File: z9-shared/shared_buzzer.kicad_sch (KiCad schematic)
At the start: 6 parts

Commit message: x
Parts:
- gave numbers to parts that had none: 6
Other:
- note added: "700 series"
- note added: "do not annotate - intended to be shared"
- note removed: "do not annotate - intended to nbe shared"
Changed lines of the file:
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@@
 		(title "l8")
 	)
-	(text "do not annotate - intended to nbe shared"
+	(text "700 series "
+		(exclude_from_sim no)
+		(at 125.222 132.334 0)
+		(effects
+			(font
+				(size 1.27 1.27)
+			)
+		)
+	)
+	(text "do not annotate - intended to be shared"
 		(exclude_from_sim no)
 		(at 159.258 131.064 0)
@@
 		(dnp no)
 		(fields_autoplaced yes)
-		(property "Reference" "Q?"
+		(property "Reference" "Q701"
 			(at 153.67 97.7899 0)
 			(effects
@@
 				)
 			)
-			(project "z9-console"
-				(path "/8d063f79-9282-4820-bcf4-1ff3c006cf08/8d0cf1ff-dd45-490a-9f6d-ad4eb4a5c201"
-					(reference "Q?")
+			(project "z9-pdm"
+				(path "/8d063f79-9282-4820-bcf4-1ff3c006cf08/c97401c5-7e03-4d93-a14f-f692468677b5"
+					(reference "Q701")
 					(unit 1)
 				)
@@
 		(dnp no)
 		(fields_autoplaced yes)
-		(property "Reference" "D?"
+		(property "Reference" "D701"
 			(at 139.7 79.6924 0)
 			(effects
@@
 				)
 			)
-			(project "z9-console"
-				(path "/8d063f79-9282-4820-bcf4-1ff3c006cf08/8d0cf1ff-dd45-490a-9f6d-ad4eb4a5c201"
-					(reference "D?")
+			(project "z9-pdm"
+				(path "/8d063f79-9282-4820-bcf4-1ff3c006cf08/c97401c5-7e03-4d93-a14f-f692468677b5"
+					(reference "D701")
 					(unit 1)
 				)
@@
 		(dnp no)
 		(fields_autoplaced yes)
-		(property "Reference" "#PWR0103"
+		(property "Reference" "#PWR0701"
 			(at 127 120.65 0)
 			(effects
@@
 				)
 			)
-			(project "z9-console"
-				(path "/8d063f79-9282-4820-bcf4-1ff3c006cf08/8d0cf1ff-dd45-490a-9f6d-ad4eb4a5c201"
-					(reference "#PWR?")
+			(project "z9-pdm"
+				(path "/8d063f79-9282-4820-bcf4-1ff3c006cf08/c97401c5-7e03-4d93-a14f-f692468677b5"
+					(reference "#PWR0701")
 					(unit 1)
 				)
@@
 		(dnp no)
 		(fields_autoplaced yes)
-		(property "Reference" "#PWR0102"
+		(property "Reference" "#PWR0702"
 			(at 149.86 72.39 0)
 			(effects
@@
 				)
 			)
-			(project "z9-console"
-				(path "/8d063f79-9282-4820-bcf4-1ff3c006cf08/8d0cf1ff-dd45-490a-9f6d-ad4eb4a5c201"
-					(reference "#PWR?")
+			(project "z9-pdm"
+				(path "/8d063f79-9282-4820-bcf4-1ff3c006cf08/c97401c5-7e03-4d93-a14f-f692468677b5"
+					(reference "#PWR0702")
 					(unit 1)
 				)
@@
 		(on_board yes)
 		(dnp no)
-		(property "Reference" "C?"
+		(property "Reference" "C701"
 			(at 129.54 77.47 90)
 			(effects
@@
 				)
 			)
-			(project "z9-console"
-				(path "/8d063f79-9282-4820-bcf4-1ff3c006cf08/8d0cf1ff-dd45-490a-9f6d-ad4eb4a5c201"
-					(reference "C?")
+			(project "z9-pdm"
+				(path "/8d063f79-9282-4820-bcf4-1ff3c006cf08/c97401c5-7e03-4d93-a14f-f692468677b5"
+					(reference "C701")
 					(unit 1)
 				)
@@
 		(dnp no)
 		(fields_autoplaced yes)
-		(property "Reference" "BZ?"
+		(property "Reference" "BZ701"
 			(at 156.21 78.7399 0)
 			(effects
@@
 				)
 			)
-			(project "z9-console"
-				(path "/8d063f79-9282-4820-bcf4-1ff3c006cf08/8d0cf1ff-dd45-490a-9f6d-ad4eb4a5c201"
-					(reference "BZ?")
+			(project "z9-pdm"
+				(path "/8d063f79-9282-4820-bcf4-1ff3c006cf08/c97401c5-7e03-4d93-a14f-f692468677b5"
+					(reference "BZ701")
 					(unit 1)
 				)
@@
 		(on_board yes)
 		(dnp no)
-		(property "Reference" "R?"
+		(property "Reference" "R704"
 			(at 129.032 110.49 90)
 			(effects
@@
 				)
 			)
-			(project "z9-console"
-				(path "/8d063f79-9282-4820-bcf4-1ff3c006cf08/8d0cf1ff-dd45-490a-9f6d-ad4eb4a5c201"
-					(reference "R?")
+			(project "z9-pdm"
+				(path "/8d063f79-9282-4820-bcf4-1ff3c006cf08/c97401c5-7e03-4d93-a14f-f692468677b5"
+					(reference "R704")
 					(unit 1)
 				)
@@
 		(on_board yes)
 		(dnp no)
-		(property "Reference" "R?"
+		(property "Reference" "R703"
 			(at 121.92 101.6 90)
 			(effects
@@
 				)
 			)
-			(project "z9-console"
-				(path "/8d063f79-9282-4820-bcf4-1ff3c006cf08/8d0cf1ff-dd45-490a-9f6d-ad4eb4a5c201"
-					(reference "R?")
+			(project "z9-pdm"
+				(path "/8d063f79-9282-4820-bcf4-1ff3c006cf08/c97401c5-7e03-4d93-a14f-f692468677b5"
+					(reference "R703")
 					(unit 1)
 				)
@@
 		(dnp no)
 		(fields_autoplaced yes)
-		(property "Reference" "#PWR0101"
+		(property "Reference" "#PWR0703"
 			(at 149.86 119.38 0)
 			(effects
@@
 				)
 			)
-			(project "z9-console"
-				(path "/8d063f79-9282-4820-bcf4-1ff3c006cf08/8d0cf1ff-dd45-490a-9f6d-ad4eb4a5c201"
-					(reference "#PWR?")
-					(unit 1)
-				)
+			(project "z9-pdm"
+				(path "/8d063f79-9282-4820-bcf4-1ff3c006cf08/c97401c5-7e03-4d93-a14f-f692468677b5"
+					(reference "#PWR0703")
+					(unit 1)
+				)

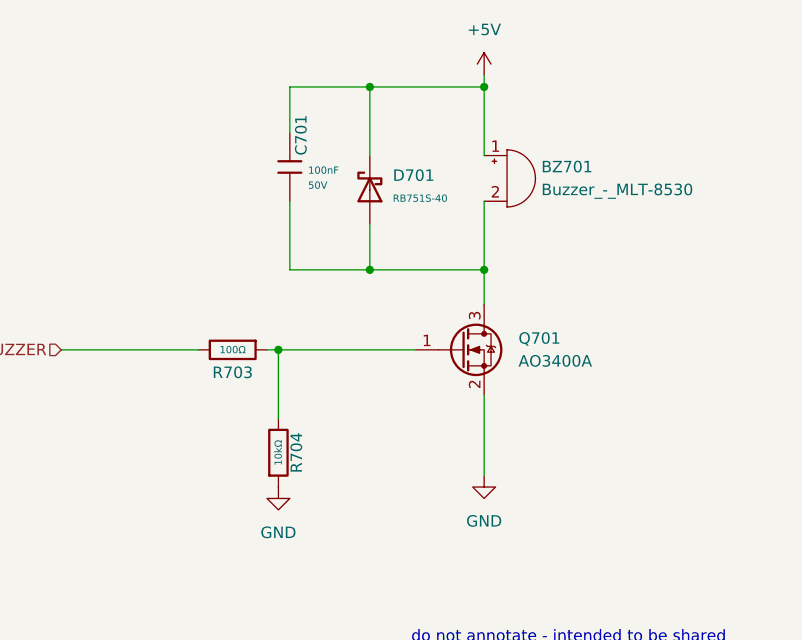
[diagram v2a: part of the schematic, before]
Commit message: lcd power switch-- add new accelerometer
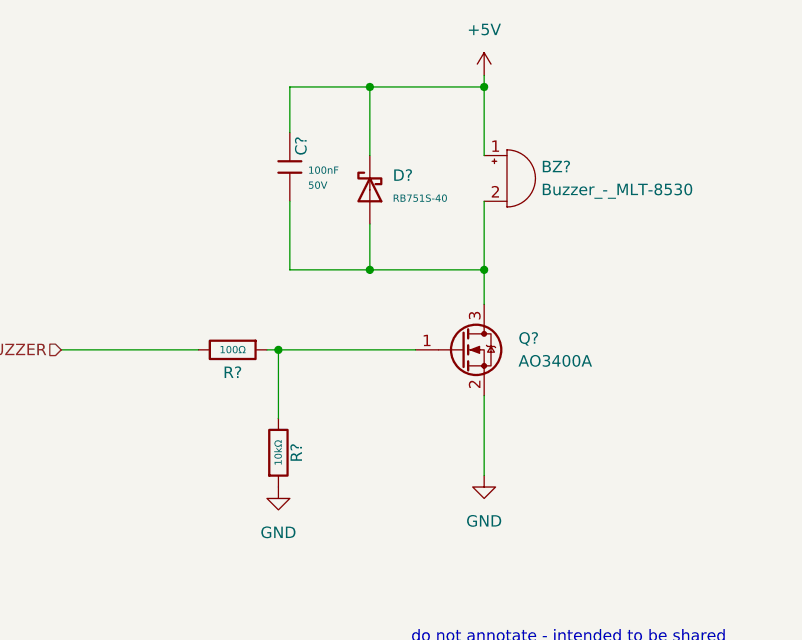
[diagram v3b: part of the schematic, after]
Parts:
- renumbered BZ701 to BZ?, C701 to C?, D701 to D?, Q701 to Q?, R704 to R?, R703 to R?
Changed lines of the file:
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@@
 		(dnp no)
 		(fields_autoplaced yes)
-		(property "Reference" "Q701"
+		(property "Reference" "Q?"
 			(at 153.67 97.7899 0)
 			(effects
@@
 				)
 			)
-			(project "z9-pdm"
-				(path "/8d063f79-9282-4820-bcf4-1ff3c006cf08/c97401c5-7e03-4d93-a14f-f692468677b5"
-					(reference "Q701")
+			(project "z9-console"
+				(path "/8d063f79-9282-4820-bcf4-1ff3c006cf08/8d0cf1ff-dd45-490a-9f6d-ad4eb4a5c201"
+					(reference "Q?")
 					(unit 1)
 				)
@@
 		(dnp no)
 		(fields_autoplaced yes)
-		(property "Reference" "D701"
+		(property "Reference" "D?"
 			(at 139.7 79.6924 0)
 			(effects
@@
 				)
 			)
-			(project "z9-pdm"
-				(path "/8d063f79-9282-4820-bcf4-1ff3c006cf08/c97401c5-7e03-4d93-a14f-f692468677b5"
-					(reference "D701")
+			(project "z9-console"
+				(path "/8d063f79-9282-4820-bcf4-1ff3c006cf08/8d0cf1ff-dd45-490a-9f6d-ad4eb4a5c201"
+					(reference "D?")
 					(unit 1)
 				)
@@
 		(dnp no)
 		(fields_autoplaced yes)
-		(property "Reference" "#PWR0701"
+		(property "Reference" "#PWR?"
 			(at 127 120.65 0)
 			(effects
@@
 				)
 			)
-			(project "z9-pdm"
-				(path "/8d063f79-9282-4820-bcf4-1ff3c006cf08/c97401c5-7e03-4d93-a14f-f692468677b5"
-					(reference "#PWR0701")
+			(project "z9-console"
+				(path "/8d063f79-9282-4820-bcf4-1ff3c006cf08/8d0cf1ff-dd45-490a-9f6d-ad4eb4a5c201"
+					(reference "#PWR?")
 					(unit 1)
 				)
@@
 		(dnp no)
 		(fields_autoplaced yes)
-		(property "Reference" "#PWR0702"
+		(property "Reference" "#PWR?"
 			(at 149.86 72.39 0)
 			(effects
@@
 				)
 			)
-			(project "z9-pdm"
-				(path "/8d063f79-9282-4820-bcf4-1ff3c006cf08/c97401c5-7e03-4d93-a14f-f692468677b5"
-					(reference "#PWR0702")
+			(project "z9-console"
+				(path "/8d063f79-9282-4820-bcf4-1ff3c006cf08/8d0cf1ff-dd45-490a-9f6d-ad4eb4a5c201"
+					(reference "#PWR?")
 					(unit 1)
 				)
@@
 		(on_board yes)
 		(dnp no)
-		(property "Reference" "C701"
+		(property "Reference" "C?"
 			(at 129.54 77.47 90)
 			(effects
@@
 				)
 			)
-			(project "z9-pdm"
-				(path "/8d063f79-9282-4820-bcf4-1ff3c006cf08/c97401c5-7e03-4d93-a14f-f692468677b5"
-					(reference "C701")
+			(project "z9-console"
+				(path "/8d063f79-9282-4820-bcf4-1ff3c006cf08/8d0cf1ff-dd45-490a-9f6d-ad4eb4a5c201"
+					(reference "C?")
 					(unit 1)
 				)
@@
 		(dnp no)
 		(fields_autoplaced yes)
-		(property "Reference" "BZ701"
+		(property "Reference" "BZ?"
 			(at 156.21 78.7399 0)
 			(effects
@@
 				)
 			)
-			(project "z9-pdm"
-				(path "/8d063f79-9282-4820-bcf4-1ff3c006cf08/c97401c5-7e03-4d93-a14f-f692468677b5"
-					(reference "BZ701")
+			(project "z9-console"
+				(path "/8d063f79-9282-4820-bcf4-1ff3c006cf08/8d0cf1ff-dd45-490a-9f6d-ad4eb4a5c201"
+					(reference "BZ?")
 					(unit 1)
 				)
@@
 		(on_board yes)
 		(dnp no)
-		(property "Reference" "R704"
+		(property "Reference" "R?"
 			(at 129.032 110.49 90)
 			(effects
@@
 				)
 			)
-			(project "z9-pdm"
-				(path "/8d063f79-9282-4820-bcf4-1ff3c006cf08/c97401c5-7e03-4d93-a14f-f692468677b5"
-					(reference "R704")
+			(project "z9-console"
+				(path "/8d063f79-9282-4820-bcf4-1ff3c006cf08/8d0cf1ff-dd45-490a-9f6d-ad4eb4a5c201"
+					(reference "R?")
 					(unit 1)
 				)
@@
 		(on_board yes)
 		(dnp no)
-		(property "Reference" "R703"
+		(property "Reference" "R?"
 			(at 121.92 101.6 90)
 			(effects
@@
 				)
 			)
-			(project "z9-pdm"
-				(path "/8d063f79-9282-4820-bcf4-1ff3c006cf08/c97401c5-7e03-4d93-a14f-f692468677b5"
-					(reference "R703")
+			(project "z9-console"
+				(path "/8d063f79-9282-4820-bcf4-1ff3c006cf08/8d0cf1ff-dd45-490a-9f6d-ad4eb4a5c201"
+					(reference "R?")
 					(unit 1)
 				)
@@
 		(dnp no)
 		(fields_autoplaced yes)
-		(property "Reference" "#PWR0703"
+		(property "Reference" "#PWR?"
 			(at 149.86 119.38 0)
 			(effects
@@
 				)
 			)
-			(project "z9-pdm"
-				(path "/8d063f79-9282-4820-bcf4-1ff3c006cf08/c97401c5-7e03-4d93-a14f-f692468677b5"
-					(reference "#PWR0703")
-					(unit 1)
-				)
+			(project "z9-console"
+				(path "/8d063f79-9282-4820-bcf4-1ff3c006cf08/8d0cf1ff-dd45-490a-9f6d-ad4eb4a5c201"
+					(reference "#PWR?")
+					(unit 1)
+				)

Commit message: change MEMS device
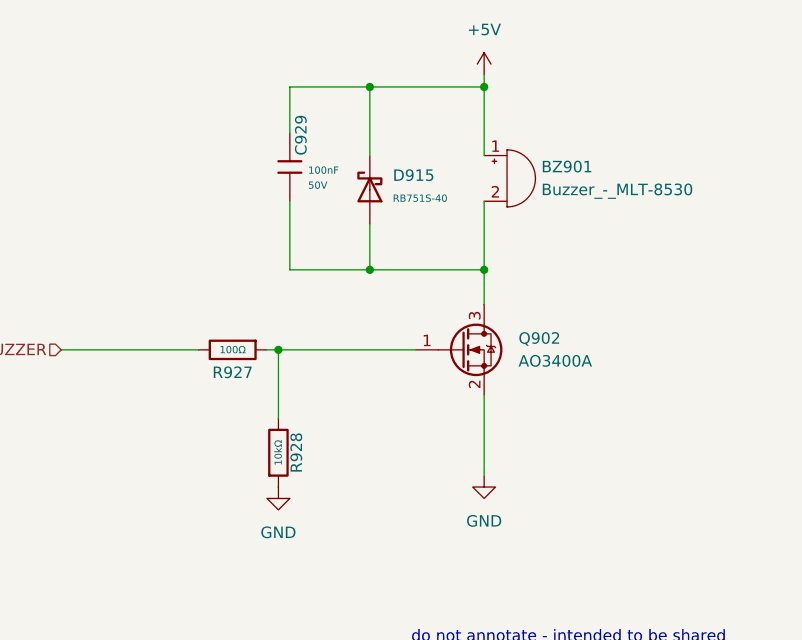
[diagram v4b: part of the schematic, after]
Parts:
- gave numbers to parts that had none: 6
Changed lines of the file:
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@@
 		(dnp no)
 		(fields_autoplaced yes)
-		(property "Reference" "Q?"
+		(property "Reference" "Q902"
 			(at 153.67 97.7899 0)
 			(effects
@@
 			(project "z9-console"
 				(path "/8d063f79-9282-4820-bcf4-1ff3c006cf08/8d0cf1ff-dd45-490a-9f6d-ad4eb4a5c201"
-					(reference "Q?")
+					(reference "Q902")
 					(unit 1)
 				)
@@
 		(dnp no)
 		(fields_autoplaced yes)
-		(property "Reference" "D?"
+		(property "Reference" "D915"
 			(at 139.7 79.6924 0)
 			(effects
@@
 			(project "z9-console"
 				(path "/8d063f79-9282-4820-bcf4-1ff3c006cf08/8d0cf1ff-dd45-490a-9f6d-ad4eb4a5c201"
-					(reference "D?")
+					(reference "D915")
 					(unit 1)
 				)
@@
 		(dnp no)
 		(fields_autoplaced yes)
-		(property "Reference" "#PWR?"
+		(property "Reference" "#PWR0946"
 			(at 127 120.65 0)
 			(effects
@@
 			(project "z9-console"
 				(path "/8d063f79-9282-4820-bcf4-1ff3c006cf08/8d0cf1ff-dd45-490a-9f6d-ad4eb4a5c201"
-					(reference "#PWR?")
+					(reference "#PWR0946")
 					(unit 1)
 				)
@@
 		(dnp no)
 		(fields_autoplaced yes)
-		(property "Reference" "#PWR?"
+		(property "Reference" "#PWR0947"
 			(at 149.86 72.39 0)
 			(effects
@@
 			(project "z9-console"
 				(path "/8d063f79-9282-4820-bcf4-1ff3c006cf08/8d0cf1ff-dd45-490a-9f6d-ad4eb4a5c201"
-					(reference "#PWR?")
+					(reference "#PWR0947")
 					(unit 1)
 				)
@@
 		(on_board yes)
 		(dnp no)
-		(property "Reference" "C?"
+		(property "Reference" "C929"
 			(at 129.54 77.47 90)
 			(effects
@@
 			(project "z9-console"
 				(path "/8d063f79-9282-4820-bcf4-1ff3c006cf08/8d0cf1ff-dd45-490a-9f6d-ad4eb4a5c201"
-					(reference "C?")
+					(reference "C929")
 					(unit 1)
 				)
@@
 		(dnp no)
 		(fields_autoplaced yes)
-		(property "Reference" "BZ?"
+		(property "Reference" "BZ901"
 			(at 156.21 78.7399 0)
 			(effects
@@
 			(project "z9-console"
 				(path "/8d063f79-9282-4820-bcf4-1ff3c006cf08/8d0cf1ff-dd45-490a-9f6d-ad4eb4a5c201"
-					(reference "BZ?")
+					(reference "BZ901")
 					(unit 1)
 				)
@@
 		(on_board yes)
 		(dnp no)
-		(property "Reference" "R?"
+		(property "Reference" "R928"
 			(at 129.032 110.49 90)
 			(effects
@@
 			(project "z9-console"
 				(path "/8d063f79-9282-4820-bcf4-1ff3c006cf08/8d0cf1ff-dd45-490a-9f6d-ad4eb4a5c201"
-					(reference "R?")
+					(reference "R928")
 					(unit 1)
 				)
@@
 		(on_board yes)
 		(dnp no)
-		(property "Reference" "R?"
+		(property "Reference" "R927"
 			(at 121.92 101.6 90)
 			(effects
@@
 			(project "z9-console"
 				(path "/8d063f79-9282-4820-bcf4-1ff3c006cf08/8d0cf1ff-dd45-490a-9f6d-ad4eb4a5c201"
-					(reference "R?")
+					(reference "R927")
 					(unit 1)
 				)
@@
 		(dnp no)
 		(fields_autoplaced yes)
-		(property "Reference" "#PWR?"
+		(property "Reference" "#PWR0948"
 			(at 149.86 119.38 0)
 			(effects
@@
 			(project "z9-console"
 				(path "/8d063f79-9282-4820-bcf4-1ff3c006cf08/8d0cf1ff-dd45-490a-9f6d-ad4eb4a5c201"
-					(reference "#PWR?")
-					(unit 1)
-				)
+					(reference "#PWR0948")
+					(unit 1)
+				)

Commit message: cleanup - change fus as test to shorten vale
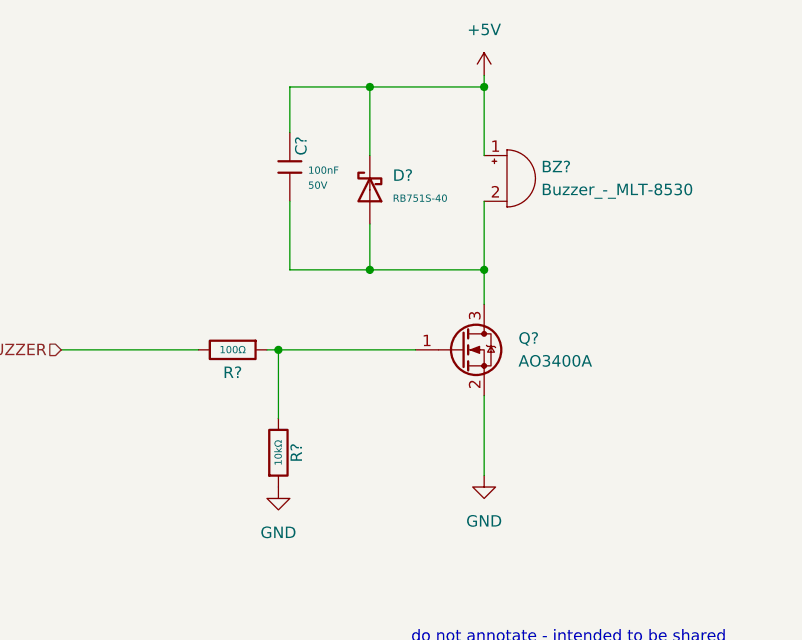
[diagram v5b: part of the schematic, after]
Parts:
- renumbered BZ901 to BZ?, C929 to C?, D915 to D?, Q902 to Q?, R928 to R?, R927 to R?
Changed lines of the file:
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@@
 		(dnp no)
 		(fields_autoplaced yes)
-		(property "Reference" "Q902"
+		(property "Reference" "Q?"
 			(at 153.67 97.7899 0)
 			(effects
@@
 				)
 			)
-			(project "z9-console"
-				(path "/8d063f79-9282-4820-bcf4-1ff3c006cf08/8d0cf1ff-dd45-490a-9f6d-ad4eb4a5c201"
-					(reference "Q902")
+			(project "z9-pdm"
+				(path "/8d063f79-9282-4820-bcf4-1ff3c006cf08/c97401c5-7e03-4d93-a14f-f692468677b5"
+					(reference "Q?")
 					(unit 1)
 				)
@@
 		(dnp no)
 		(fields_autoplaced yes)
-		(property "Reference" "D915"
+		(property "Reference" "D?"
 			(at 139.7 79.6924 0)
 			(effects
@@
 				)
 			)
-			(project "z9-console"
-				(path "/8d063f79-9282-4820-bcf4-1ff3c006cf08/8d0cf1ff-dd45-490a-9f6d-ad4eb4a5c201"
-					(reference "D915")
+			(project "z9-pdm"
+				(path "/8d063f79-9282-4820-bcf4-1ff3c006cf08/c97401c5-7e03-4d93-a14f-f692468677b5"
+					(reference "D?")
 					(unit 1)
 				)
@@
 		(dnp no)
 		(fields_autoplaced yes)
-		(property "Reference" "#PWR0946"
+		(property "Reference" "#PWR?"
 			(at 127 120.65 0)
 			(effects
@@
 				)
 			)
-			(project "z9-console"
-				(path "/8d063f79-9282-4820-bcf4-1ff3c006cf08/8d0cf1ff-dd45-490a-9f6d-ad4eb4a5c201"
-					(reference "#PWR0946")
+			(project "z9-pdm"
+				(path "/8d063f79-9282-4820-bcf4-1ff3c006cf08/c97401c5-7e03-4d93-a14f-f692468677b5"
+					(reference "#PWR?")
 					(unit 1)
 				)
@@
 		(dnp no)
 		(fields_autoplaced yes)
-		(property "Reference" "#PWR0947"
+		(property "Reference" "#PWR?"
 			(at 149.86 72.39 0)
 			(effects
@@
 				)
 			)
-			(project "z9-console"
-				(path "/8d063f79-9282-4820-bcf4-1ff3c006cf08/8d0cf1ff-dd45-490a-9f6d-ad4eb4a5c201"
-					(reference "#PWR0947")
+			(project "z9-pdm"
+				(path "/8d063f79-9282-4820-bcf4-1ff3c006cf08/c97401c5-7e03-4d93-a14f-f692468677b5"
+					(reference "#PWR?")
 					(unit 1)
 				)
@@
 		(on_board yes)
 		(dnp no)
-		(property "Reference" "C929"
+		(property "Reference" "C?"
 			(at 129.54 77.47 90)
 			(effects
@@
 				)
 			)
-			(project "z9-console"
-				(path "/8d063f79-9282-4820-bcf4-1ff3c006cf08/8d0cf1ff-dd45-490a-9f6d-ad4eb4a5c201"
-					(reference "C929")
+			(project "z9-pdm"
+				(path "/8d063f79-9282-4820-bcf4-1ff3c006cf08/c97401c5-7e03-4d93-a14f-f692468677b5"
+					(reference "C?")
 					(unit 1)
 				)
@@
 		(dnp no)
 		(fields_autoplaced yes)
-		(property "Reference" "BZ901"
+		(property "Reference" "BZ?"
 			(at 156.21 78.7399 0)
 			(effects
@@
 				)
 			)
-			(project "z9-console"
-				(path "/8d063f79-9282-4820-bcf4-1ff3c006cf08/8d0cf1ff-dd45-490a-9f6d-ad4eb4a5c201"
-					(reference "BZ901")
+			(project "z9-pdm"
+				(path "/8d063f79-9282-4820-bcf4-1ff3c006cf08/c97401c5-7e03-4d93-a14f-f692468677b5"
+					(reference "BZ?")
 					(unit 1)
 				)
@@
 		(on_board yes)
 		(dnp no)
-		(property "Reference" "R928"
+		(property "Reference" "R?"
 			(at 129.032 110.49 90)
 			(effects
@@
 				)
 			)
-			(project "z9-console"
-				(path "/8d063f79-9282-4820-bcf4-1ff3c006cf08/8d0cf1ff-dd45-490a-9f6d-ad4eb4a5c201"
-					(reference "R928")
+			(project "z9-pdm"
+				(path "/8d063f79-9282-4820-bcf4-1ff3c006cf08/c97401c5-7e03-4d93-a14f-f692468677b5"
+					(reference "R?")
 					(unit 1)
 				)
@@
 		(on_board yes)
 		(dnp no)
-		(property "Reference" "R927"
+		(property "Reference" "R?"
 			(at 121.92 101.6 90)
 			(effects
@@
 				)
 			)
-			(project "z9-console"
-				(path "/8d063f79-9282-4820-bcf4-1ff3c006cf08/8d0cf1ff-dd45-490a-9f6d-ad4eb4a5c201"
-					(reference "R927")
+			(project "z9-pdm"
+				(path "/8d063f79-9282-4820-bcf4-1ff3c006cf08/c97401c5-7e03-4d93-a14f-f692468677b5"
+					(reference "R?")
 					(unit 1)
 				)
@@
 		(dnp no)
 		(fields_autoplaced yes)
-		(property "Reference" "#PWR0948"
+		(property "Reference" "#PWR?"
 			(at 149.86 119.38 0)
 			(effects
@@
 				)
 			)
-			(project "z9-console"
-				(path "/8d063f79-9282-4820-bcf4-1ff3c006cf08/8d0cf1ff-dd45-490a-9f6d-ad4eb4a5c201"
-					(reference "#PWR0948")
-					(unit 1)
-				)
+			(project "z9-pdm"
+				(path "/8d063f79-9282-4820-bcf4-1ff3c006cf08/c97401c5-7e03-4d93-a14f-f692468677b5"
+					(reference "#PWR?")
+					(unit 1)
+				)
